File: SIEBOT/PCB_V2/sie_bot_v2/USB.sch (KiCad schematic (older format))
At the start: 34 parts, among them J3 USB_2A, U4 GL850G, U5 RCLAMP0502B, U6 RCLAMP0502B, U7 RCLAMP0502B, U8 RCLAMP0502B, U9 MCP130, X2 12MHz

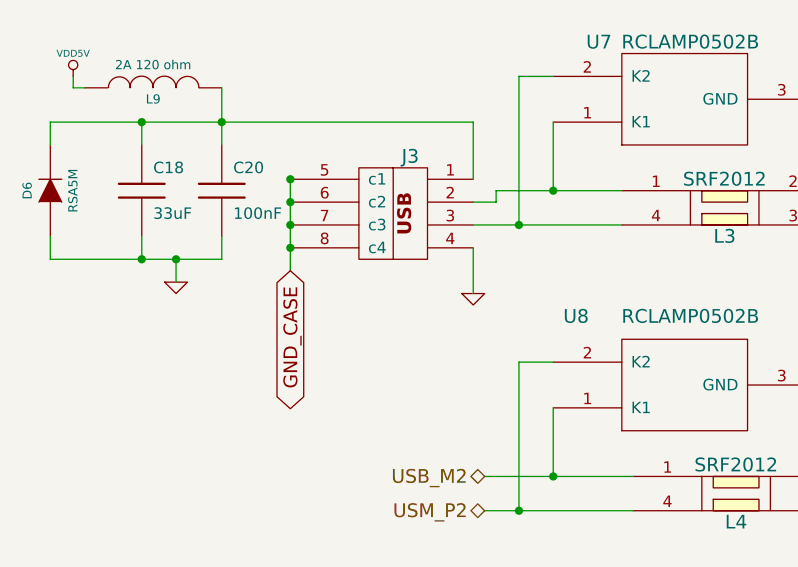
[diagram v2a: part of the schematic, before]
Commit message: Inicio de ruteo de los cambios realizados en el esquematico
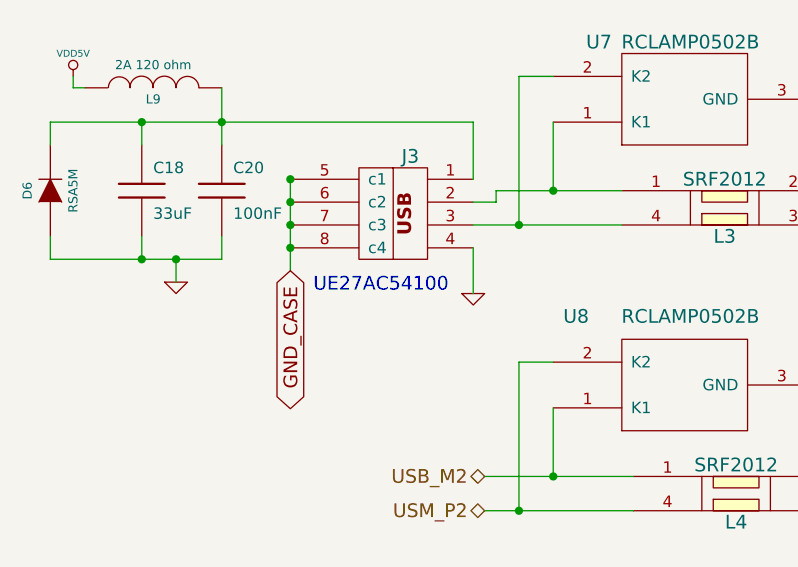
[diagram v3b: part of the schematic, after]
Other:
- note added: "UE27AC54100"
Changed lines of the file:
@@
-EESchema Schematic File Version 2  date Fri 10 Feb 2012 05:02:18 PM COT
+EESchema Schematic File Version 2  date Fri 10 Feb 2012 06:23:52 PM COT
 LIBS:con-jack
 LIBS:adm3101e
@@
 Comment4 ""
 $EndDescr
+Text Notes 1700 2100 0    60   ~ 0
+UE27AC54100
 Text Notes 9600 2850 0    60   ~ 0
 JP4, se utiliza para programar\nlos bits OTP (modo usb device)
@@
 USM_P2
 $Comp
-L VDDIO_3V3 #PWR133
+L VDDIO_3V3 #PWR0110
 U 1 1 4E5BAA82
 P 6500 1750
-F 0 "#PWR133" H 6500 1850 30  0001 C CNN
+F 0 "#PWR0110" H 6500 1850 30  0001 C CNN
 F 1 "VDDIO_3V3" H 6500 1850 30  0000 C CNN
 	1    6500 1750
@@
 $EndComp
 $Comp
-L GND #PWR129
+L GND #PWR0111
 U 1 1 4E43139E
 P 4950 3200
-F 0 "#PWR129" H 4950 3200 30  0001 C CNN
+F 0 "#PWR0111" H 4950 3200 30  0001 C CNN
 F 1 "GND" H 4950 3130 30  0001 C CNN
 	1    4950 3200
@@
 USBH_P33VD
 $Comp
-L GND #PWR134
+L GND #PWR0112
 U 1 1 4E41C8A5
 P 6700 3350
-F 0 "#PWR134" H 6700 3350 30  0001 C CNN
+F 0 "#PWR0112" H 6700 3350 30  0001 C CNN
 F 1 "GND" H 6700 3280 30  0001 C CNN
 	1    6700 3350
@@
 $EndComp
 $Comp
-L GND #PWR131
+L GND #PWR0113
 U 1 1 4E41C7BC
 P 5500 3750
-F 0 "#PWR131" H 5500 3750 30  0001 C CNN
+F 0 "#PWR0113" H 5500 3750 30  0001 C CNN
 F 1 "GND" H 5500 3680 30  0001 C CNN
 	1    5500 3750
@@
 $EndComp
 $Comp
-L GND #PWR125
+L GND #PWR0114
 U 1 1 4E4157F8
 P 3950 4850
-F 0 "#PWR125" H 3950 4850 30  0001 C CNN
+F 0 "#PWR0114" H 3950 4850 30  0001 C CNN
 F 1 "GND" H 3950 4780 30  0001 C CNN
 	1    3950 4850
@@
 $EndComp
 $Comp
-L GND #PWR124
+L GND #PWR0115
 U 1 1 4E4157E9
 P 3950 3800
-F 0 "#PWR124" H 3950 3800 30  0001 C CNN
+F 0 "#PWR0115" H 3950 3800 30  0001 C CNN
 F 1 "GND" H 3950 3730 30  0001 C CNN
 	1    3950 3800
@@
 $EndComp
 $Comp
-L GND #PWR127
+L GND #PWR0116
 U 1 1 4E4157C0
 P 4000 2650
-F 0 "#PWR127" H 4000 2650 30  0001 C CNN
+F 0 "#PWR0116" H 4000 2650 30  0001 C CNN
 F 1 "GND" H 4000 2580 30  0001 C CNN
 	1    4000 2650
@@
 $EndComp
 $Comp
-L GND #PWR126
+L GND #PWR0117
 U 1 1 4E4157B3
 P 4000 1350
-F 0 "#PWR126" H 4000 1350 30  0001 C CNN
+F 0 "#PWR0117" H 4000 1350 30  0001 C CNN
 F 1 "GND" H 4000 1280 30  0001 C CNN
 	1    4000 1350
@@
 $EndComp
 $Comp
-L GND #PWR122
+L GND #PWR0118
 U 1 1 4E415157
 P 1100 2050
-F 0 "#PWR122" H 1100 2050 30  0001 C CNN
+F 0 "#PWR0118" H 1100 2050 30  0001 C CNN
 F 1 "GND" H 1100 1980 30  0001 C CNN
 	1    1100 2050
@@
 $EndComp
 $Comp
-L GND #PWR123
+L GND #PWR0119
 U 1 1 4E414F30
 P 2400 2100
-F 0 "#PWR123" H 2400 2100 30  0001 C CNN
+F 0 "#PWR0119" H 2400 2100 30  0001 C CNN
 F 1 "GND" H 2400 2030 30  0001 C CNN
 	1    2400 2100
@@
 $EndComp
 $Comp
-L VDD5V #PWR121
+L VDD5V #PWR0120
 U 1 1 4E414E3D
 P 650 1150
-F 0 "#PWR121" H 650 1250 30  0001 C CNN
+F 0 "#PWR0120" H 650 1250 30  0001 C CNN
 F 1 "VDD5V" H 650 1250 30  0000 C CNN
 	1    650  1150
@@
 $EndComp
 $Comp
-L GND #PWR136
+L GND #PWR0121
 U 1 1 4E3C4430
 P 7400 1400
-F 0 "#PWR136" H 7400 1400 30  0001 C CNN
+F 0 "#PWR0121" H 7400 1400 30  0001 C CNN
 F 1 "GND" H 7400 1330 30  0001 C CNN
 	1    7400 1400
@@
 $EndComp
 $Comp
-L VDD5V #PWR135
+L VDD5V #PWR0122
 U 1 1 4E3C4429
 P 7400 800
-F 0 "#PWR135" H 7400 900 30  0001 C CNN
+F 0 "#PWR0122" H 7400 900 30  0001 C CNN
 F 1 "VDD5V" H 7400 900 30  0000 C CNN
 	1    7400 800
@@
 $EndComp
 $Comp
-L VDD5V #PWR140
+L VDD5V #PWR0123
 U 1 1 4E3C4418
 P 9000 2500
-F 0 "#PWR140" H 9000 2600 30  0001 C CNN
+F 0 "#PWR0123" H 9000 2600 30  0001 C CNN
 F 1 "VDD5V" H 9000 2600 30  0000 C CNN
 	1    9000 2500
@@
 $EndComp
 $Comp
-L GND #PWR138
+L GND #PWR0124
 U 1 1 4E3C436B
 P 7900 1600
-F 0 "#PWR138" H 7900 1600 30  0001 C CNN
+F 0 "#PWR0124" H 7900 1600 30  0001 C CNN
 F 1 "GND" H 7900 1530 30  0001 C CNN
 	1    7900 1600
@@
 USBH_P33V
 $Comp
-L VDD5V #PWR141
+L VDD5V #PWR0125
 U 1 1 4E3C4207
 P 9000 2900
-F 0 "#PWR141" H 9000 3000 30  0001 C CNN
+F 0 "#PWR0125" H 9000 3000 30  0001 C CNN
 F 1 "VDD5V" H 9000 3000 30  0000 C CNN
 	1    9000 2900
@@
 USBH_P33V
 $Comp
-L GND #PWR142
+L GND #PWR0126
 U 1 1 4E3C3A60
 P 9300 5550
-F 0 "#PWR142" H 9300 5550 30  0001 C CNN
+F 0 "#PWR0126" H 9300 5550 30  0001 C CNN
 F 1 "GND" H 9300 5480 30  0001 C CNN
 	1    9300 5550
@@
 $EndComp
 $Comp
-L GND #PWR137
+L GND #PWR0127
 U 1 1 4E3C3A56
 P 7400 5550
-F 0 "#PWR137" H 7400 5550 30  0001 C CNN
+F 0 "#PWR0127" H 7400 5550 30  0001 C CNN
 F 1 "GND" H 7400 5480 30  0001 C CNN
 	1    7400 5550
@@
 andres.calderon@emqbit.com\n
 $Comp
-L GND #PWR132
+L GND #PWR0128
 U 1 1 4E3C3807
 P 5900 2300
-F 0 "#PWR132" H 5900 2300 30  0001 C CNN
+F 0 "#PWR0128" H 5900 2300 30  0001 C CNN
 F 1 "GND" H 5900 2230 30  0001 C CNN
 	1    5900 2300
@@
 $EndComp
 $Comp
-L GND #PWR143
+L GND #PWR0129
 U 1 1 4E3C36BE
 P 9800 3550
-F 0 "#PWR143" H 9800 3550 30  0001 C CNN
+F 0 "#PWR0129" H 9800 3550 30  0001 C CNN
 F 1 "GND" H 9800 3480 30  0001 C CNN
 	1    9800 3550
@@
 X1
 $Comp
-L GND #PWR139
+L GND #PWR0130
 U 1 1 4E3C222B
 P 8900 3700
-F 0 "#PWR139" H 8900 3700 30  0001 C CNN
+F 0 "#PWR0130" H 8900 3700 30  0001 C CNN
 F 1 "GND" H 8900 3630 30  0001 C CNN
 	1    8900 3700
@@
 USB_DM2
 $Comp
-L GND #PWR128
+L GND #PWR0131
 U 1 1 4E3C212B
 P 4650 4250
-F 0 "#PWR128" H 4650 4250 30  0001 C CNN
+F 0 "#PWR0131" H 4650 4250 30  0001 C CNN
 F 1 "GND" H 4650 4180 30  0001 C CNN
 	1    4650 4250
@@
 $EndComp
 $Comp
-L GND #PWR130
+L GND #PWR0132
 U 1 1 4E3C206C
 P 5250 4250
-F 0 "#PWR130" H 5250 4250 30  0001 C CNN
+F 0 "#PWR0132" H 5250 4250 30  0001 C CNN
 F 1 "GND" H 5250 4180 30  0001 C CNN
 	1    5250 4250

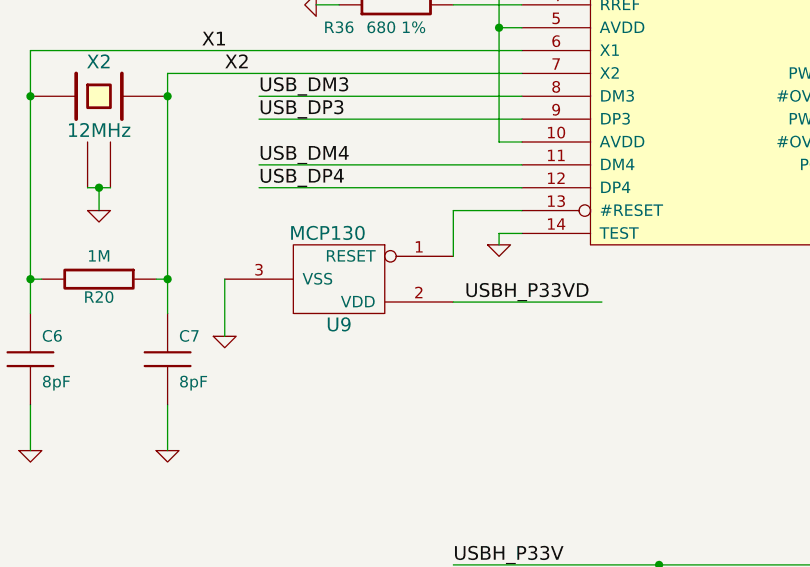
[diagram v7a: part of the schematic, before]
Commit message: Modificacion del reset del hub USB ahora el IMX233 controla el reset
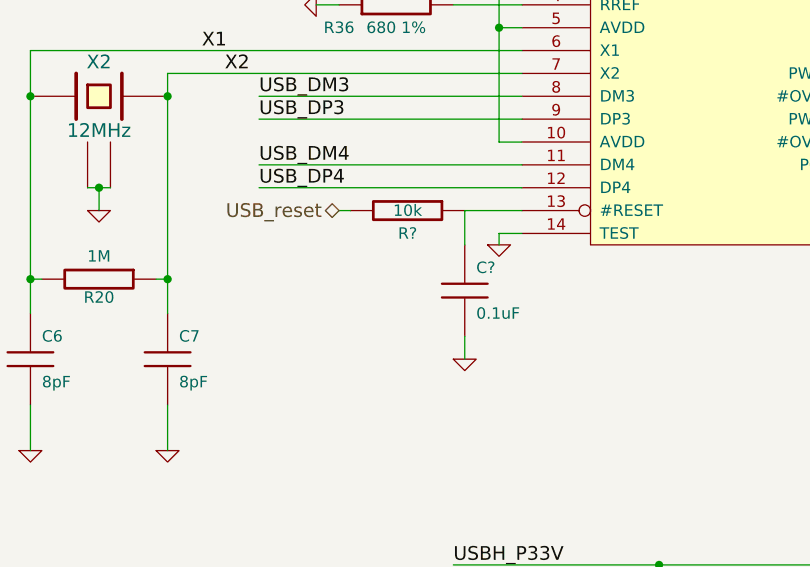
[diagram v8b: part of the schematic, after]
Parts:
- removed U9: MCP130, SOT23B-3, symbol MCP130
- added C?: 0.1uF, SM0603, symbol C
- added R?: 10k, SM0603, symbol R
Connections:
- net labels added: USB_reset
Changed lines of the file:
@@
-EESchema Schematic File Version 2  date Sat 18 Feb 2012 11:36:23 AM COT
+EESchema Schematic File Version 2  date sáb 03 mar 2012 09:20:54 COT
 LIBS:con-jack
 LIBS:adm3101e
@@
 LIBS:zxmhc3f381n8
 LIBS:i.mx233stamp-cache
-EELAYER 25  0
+EELAYER 24  0
 EELAYER END
 $Descr A4 11700 8267
-encoding utf-8
 Sheet 5 5
 Title ""
-Date "18 feb 2012"
+Date "3 mar 2012"
 Rev ""
 Comp ""
@@
 Comment4 ""
 $EndDescr
-Text Notes 1700 2100 0    60   ~ 0
-UE27AC54100
-Text Notes 9600 2850 0    60   ~ 0
-JP4, se utiliza para programar\nlos bits OTP (modo usb device)
+Text HLabel 6000 3200 0    60   BiDi ~ 0
+USB_reset
+Wire Wire Line
+	6050 3200 6000 3200
+Wire Wire Line
+	6550 3350 6550 3200
 Connection ~ 10450 2600
 Wire Wire Line
@@
 Wire Wire Line
 	6700 3350 6700 3300
-Wire Wire Line
-	6800 3200 6500 3200
-Wire Wire Line
-	6500 3200 6500 3400
 Wire Wire Line
 	6800 2600 5250 2600
@@
 	6000 2300 5900 2300
 Wire Wire Line
-	5500 3500 5500 3750
-Wire Wire Line
-	7150 3600 6500 3600
-Wire Wire Line
 	3050 1650 2500 1650
 Wire Wire Line
@@
 	9800 2200 8600 2200
 Connection ~ 10450 2000
+Wire Wire Line
+	6550 3850 6550 3750
+Wire Wire Line
+	6550 3200 6800 3200
+$Comp
+L C C?
+U 1 1 4F522649
+P 6550 3550
+F 0 "C?" H 6600 3650 50  0000 L CNN
+F 1 "0.1uF" H 6600 3450 50  0000 L CNN
+F 2 "SM0603" H 6550 3550 60  0001 C CNN
+	1    6550 3550
+	1    0    0    -1
+$EndComp
+$Comp
+L GND #PWR?
+U 1 1 4F522478
+P 6550 3850
+F 0 "#PWR?" H 6550 3850 30  0001 C CNN
+F 1 "GND" H 6550 3780 30  0001 C CNN
+	1    6550 3850
+	1    0    0    -1
+$EndComp
+$Comp
+L R R?
+U 1 1 4F522458
+P 6300 3200
+F 0 "R?" V 6400 3200 50  0000 C CNN
+F 1 "10k" V 6300 3200 50  0000 C CNN
+F 2 "SM0603" H 6300 3200 60  0001 C CNN
+	1    6300 3200
+	0    1    1    0
+$EndComp
+Text Notes 1700 2100 0    60   ~ 0
+UE27AC54100
+Text Notes 9600 2850 0    60   ~ 0
+JP4, se utiliza para programar\nlos bits OTP (modo usb device)
 Text Notes 9700 1500 0    60   ~ 0
 R42, R43, se deben montar \ndespués de configurar el imx233 \npara iniciar desde la SD.
@@
 	1    0    0    -1
 $EndComp
-Text Label 6550 3600 0    60   ~ 0
-USBH_P33VD
 $Comp
 L GND #PWR0114
@@
 	1    0    0    -1
 $EndComp
-$Comp
-L GND #PWR0115
-U 1 1 4E41C7BC
-P 5500 3750
-F 0 "#PWR0115" H 5500 3750 30  0001 C CNN
-F 1 "GND" H 5500 3680 30  0001 C CNN
-	1    5500 3750
-	1    0    0    -1
-$EndComp
 Text Label 5500 2600 0    60   ~ 0
 X2
 $Comp
-L MCP130 U9
-U 1 1 4E41C620
-P 5100 4650
-F 0 "U9" V 4150 5550 60  0000 C CNN
-F 1 "MCP130" V 3750 5500 60  0000 C CNN
-F 2 "SOT23B-3" H 5100 4650 60  0001 C CNN
-	1    5100 4650
-	0    1    1    0
-$EndComp
-$Comp
 L INDUCTOR L9
